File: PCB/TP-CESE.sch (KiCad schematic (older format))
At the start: 46 parts, among them J1 Screw_Terminal_01x04, J3 Screw_Terminal_01x02, J4 Conn_01x05_Male, J5 test, Q1 IRF540N, Q2 IRF540N, Q3 IRF540N, Q4 IRF540N, U1 4N25, U2 4N25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

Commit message: Correcciones Realizadas
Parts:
- D1, D2, D3, D4: footprint Diode_SMD:D_SC-80_HandSoldering -> Diode_THT:D_DO-35_SOD27_P7.62mm_Horizontal
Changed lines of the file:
@@
 Comp "Sebastian Herrera-Inquinoa-Conicet"
 Comment1 "Revisores:Carlos Carreño Romano,Diego Brengi"
-Comment2 "Licencia:El autor autoriza su uso "
+Comment2 "Licencia: Licencia BSD (proyecto  CIAA)"
 Comment3 ""
 Comment4 ""
@@
 F 0 "D1" V 7050 2750 50  0000 L CNN
 F 1 "1N4148" H 7150 2550 50  0000 L CNN
-F 2 "Diode_SMD:D_SC-80_HandSoldering" H 7200 2700 50  0001 C CNN
+F 2 "Diode_THT:D_DO-35_SOD27_P7.62mm_Horizontal" H 7200 2700 50  0001 C CNN
 F 3 "https://www.onsemi.com/pub/Collateral/1N914-D.PDF" H 7200 2700 50  0001 C CNN
 F 4 "1N4148FS-ND" V 7200 2700 50  0001 C CNN "Digikey#"
@@
 F 0 "D3" V 7550 2750 50  0000 L CNN
 F 1 "1N4148" H 7650 2600 50  0000 L CNN
-F 2 "Diode_SMD:D_SC-80_HandSoldering" H 7700 2700 50  0001 C CNN
+F 2 "Diode_THT:D_DO-35_SOD27_P7.62mm_Horizontal" H 7700 2700 50  0001 C CNN
 F 3 "https://www.onsemi.com/pub/Collateral/1N914-D.PDF" H 7700 2700 50  0001 C CNN
 F 4 "1N4148FS-ND" V 7700 2700 50  0001 C CNN "Digikey#"
@@
 F 0 "D4" V 7800 2750 50  0000 L CNN
 F 1 "1N4148" H 7900 2600 50  0000 L CNN
-F 2 "Diode_SMD:D_SC-80_HandSoldering" H 7950 2700 50  0001 C CNN
+F 2 "Diode_THT:D_DO-35_SOD27_P7.62mm_Horizontal" H 7950 2700 50  0001 C CNN
 F 3 "https://www.onsemi.com/pub/Collateral/1N914-D.PDF" H 7950 2700 50  0001 C CNN
 F 4 "1N4148FS-ND" V 7950 2700 50  0001 C CNN "digikey#"
@@
 F 0 "D2" V 7300 2750 50  0000 L CNN
 F 1 "1N4148" H 7400 2600 50  0000 L CNN
-F 2 "Diode_SMD:D_SC-80_HandSoldering" H 7450 2700 50  0001 C CNN
+F 2 "Diode_THT:D_DO-35_SOD27_P7.62mm_Horizontal" H 7450 2700 50  0001 C CNN
 F 3 "https://www.onsemi.com/pub/Collateral/1N914-D.PDF" H 7450 2700 50  0001 C CNN
 F 4 "1N4148FS-ND" V 7450 2700 50  0001 C CNN "Digikey#"
@@
 U 1 1 5F8D2067
 P 7900 5700
-F 0 "H1" H 8000 5746 50  0000 L CNN
+F 0 "H1" H 8000 5746 50  0001 L CNN
 F 1 "MountingHole" H 8000 5655 50  0000 L CNN
 F 2 "MountingHole:MountingHole_2.2mm_M2_DIN965_Pad" H 7900 5700 50  0001 C CNN
@@
 U 1 1 5F8D3331
 P 7900 6000
-F 0 "H2" H 8000 6046 50  0000 L CNN
+F 0 "H2" H 8000 6046 50  0001 L CNN
 F 1 "MountingHole" H 8000 5955 50  0000 L CNN
 F 2 "MountingHole:MountingHole_2.2mm_M2_DIN965_Pad" H 7900 6000 50  0001 C CNN
@@
 U 1 1 5F8D3884
 P 8650 6000
-F 0 "H4" H 8750 6046 50  0000 L CNN
+F 0 "H4" H 8750 6046 50  0001 L CNN
 F 1 "MountingHole" H 8750 5955 50  0000 L CNN
 F 2 "MountingHole:MountingHole_2.2mm_M2_DIN965_Pad" H 8650 6000 50  0001 C CNN
@@
 U 1 1 5F8D3E5A
 P 8650 5700
-F 0 "H3" H 8750 5746 50  0000 L CNN
+F 0 "H3" H 8750 5746 50  0001 L CNN
 F 1 "MountingHole" H 8750 5655 50  0000 L CNN
 F 2 "MountingHole:MountingHole_2.2mm_M2_DIN965_Pad" H 8650 5700 50  0001 C CNN
@@
 U 1 1 5FA19856
 P 9900 5500
-F 0 "FID2" H 9985 5546 50  0000 L CNN
+F 0 "FID2" H 9985 5546 50  0001 L CNN
 F 1 "Fiducial" H 9985 5455 50  0000 L CNN
 F 2 "Fiducial:Fiducial_1mm_Mask2mm" H 9900 5500 50  0001 C CNN
@@
 U 1 1 5FA1A33A
 P 10350 5500
-F 0 "FID3" H 10435 5546 50  0000 L CNN
+F 0 "FID3" H 10435 5546 50  0001 L CNN
 F 1 "Fiducial" H 10435 5455 50  0000 L CNN
 F 2 "Fiducial:Fiducial_1mm_Mask2mm" H 10350 5500 50  0001 C CNN
@@
 	1    0    0    -1
 $EndComp
+$Comp
+L Poncho_Esqueleto:Logo_Poncho #G1
+U 1 1 5F9C2AF2
+P 8050 5000
+F 0 "#G1" H 8000 4600 60  0001 C CNN
+F 1 "Logo_Poncho" H 8250 4600 60  0001 C CNN
+F 2 "Poncho_Esqueleto:Logo_Poncho" H 7950 4550 60  0000 C CNN
+F 3 "" H 8050 5000 60  0000 C CNN
+	1    8050 5000
+	1    0    0    -1
+$EndComp

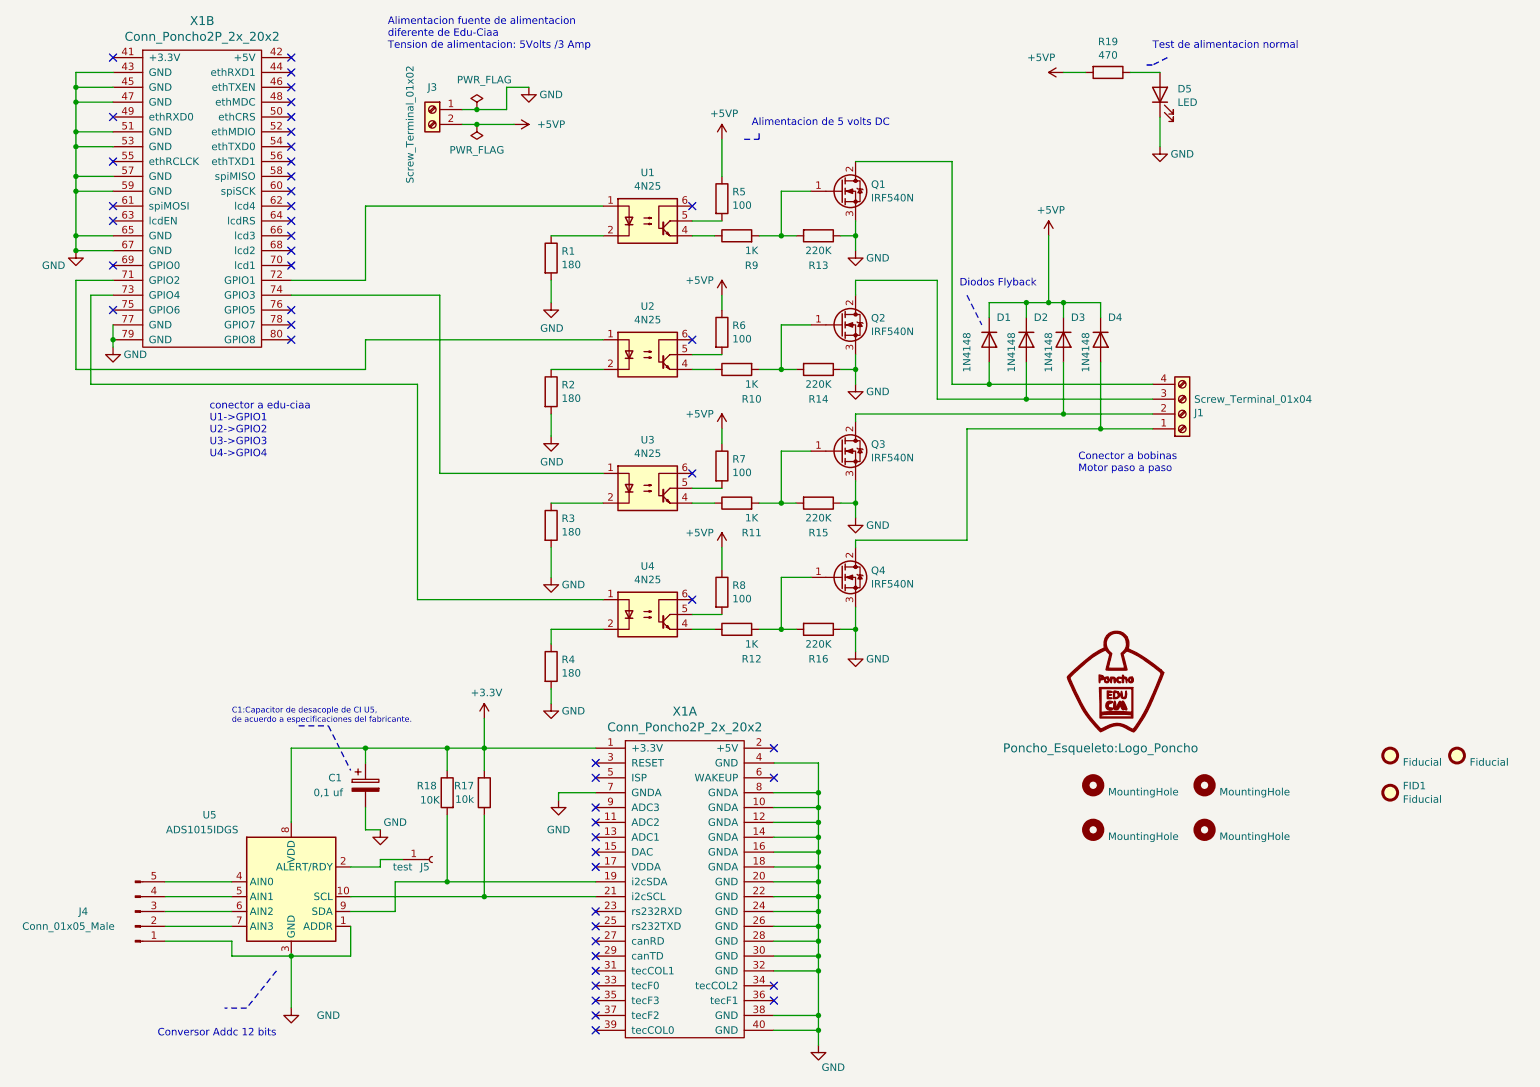
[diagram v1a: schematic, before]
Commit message: Se agrga integrado L297 , para manejo de motor paso a paso, se sacan los optoacopladores ya que el L297 maneja directamente los Irf
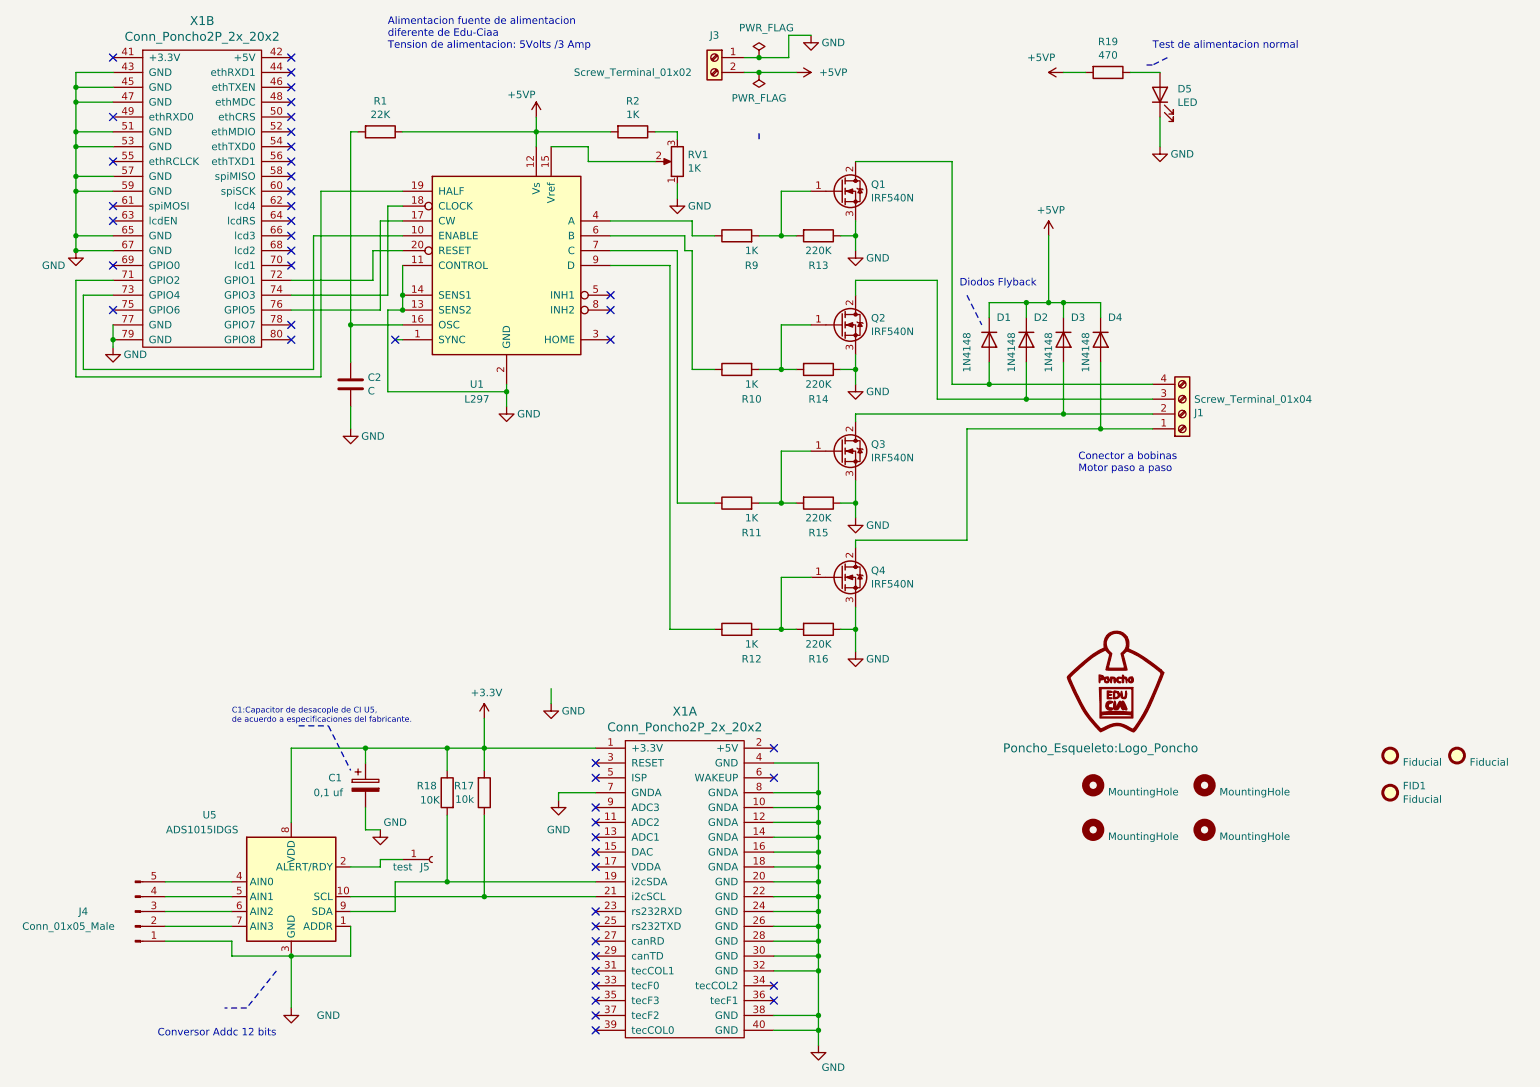
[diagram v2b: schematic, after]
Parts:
- removed R3, R4: 180, Resistor_SMD:R_0805_2012Metric_Pad1.20x1.40mm_HandSolder, symbol Device:R
- removed R5, R6, R7, R8: 100, Resistor_SMD:R_0805_2012Metric_Pad1.20x1.40mm_HandSolder, symbol Device:R
- removed U1, U2, U3, U4: 4N25, Package_DIP:DIP-6_W7.62mm, symbol Isolator:4N25
- added C2: C, Capacitor_THT:C_Disc_D3.0mm_W1.6mm_P2.50mm, symbol Device:C
- added RV1: 1K, Potentiometer_THT:Potentiometer_Bourns_3299W_Vertical, symbol Device:R_POT
- added U1: L297, Package_DIP:DIP-20_W7.62mm_Socket_LongPads, symbol Driver_Motor:L297
- D5: footprint LED_SMD:LED_0805_2012Metric_Pad1.15x1.40mm_HandSolder -> LED_THT:LED_D3.0mm_Clear
- R1: value 180 -> 22K; footprint Resistor_SMD:R_0805_2012Metric_Pad1.20x1.40mm_HandSolder -> Resistor_THT:R_Axial_DIN0207_L6.3mm_D2.5mm_P7.62mm_Horizontal
- R10, R11, R12, R13, R14, R15, R16, R17, R18, R19, R9: footprint Resistor_SMD:R_0805_2012Metric_Pad1.20x1.40mm_HandSolder -> Resistor_THT:R_Axial_DIN0207_L6.3mm_D2.5mm_P7.62mm_Horizontal
- R2: value 180 -> 1K; footprint Resistor_SMD:R_0805_2012Metric_Pad1.20x1.40mm_HandSolder -> Resistor_THT:R_Axial_DIN0207_L6.3mm_D2.5mm_P7.62mm_Horizontal
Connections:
- net +5VP: now also R1.1, R2.2, U1.12 (Vs)
- net GND: now also C2.2, RV1.1, U1.11 (CONTROL), U1.13 (SENS2), U1.14 (SENS1), U1.2 (GND); no longer R1.2, R2.2
- net at X1.72 (GPIO1): now also U1.20 (RESET)
- net at R9.1: now also U1.4 (A)
- net at X1.71 (GPIO2): now also U1.19 (HALF)
- net at R2.1: now also RV1.3
- net at R10.1: now also U1.6 (B)
- net at X1.74 (GPIO3): now also U1.18 (CLOCK)
- net at R11.1: now also U1.7 (C)
- net at X1.73 (GPIO4): now also U1.10 (ENABLE)
- net at R12.1: now also U1.9 (D)
- net at X1.76 (GPIO5): now also U1.17 (CW)
- new net: RV1.2, U1.15 (Vref)
- new net: C2.1, R1.2, U1.16 (OSC)
- no-connect marks 49 -> 48
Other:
- note removed: "Alimentacion de 5 volts DC \n\n"
- note removed: "conector a edu-ciaa\nU1->GPIO1\nU2->GPIO2\nU3->GPIO3\nU4->GPIO4"
- moved on the sheet: J3
